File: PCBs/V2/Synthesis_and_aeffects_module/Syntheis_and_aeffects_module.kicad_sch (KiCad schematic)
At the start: 36 parts, among them J1(AudioJack)1 Conn_01x03, J2(IN)1 IN, J3(OUT)1 OUT, U1 STM32H750VBTx, U2 TPA6110A2DGN

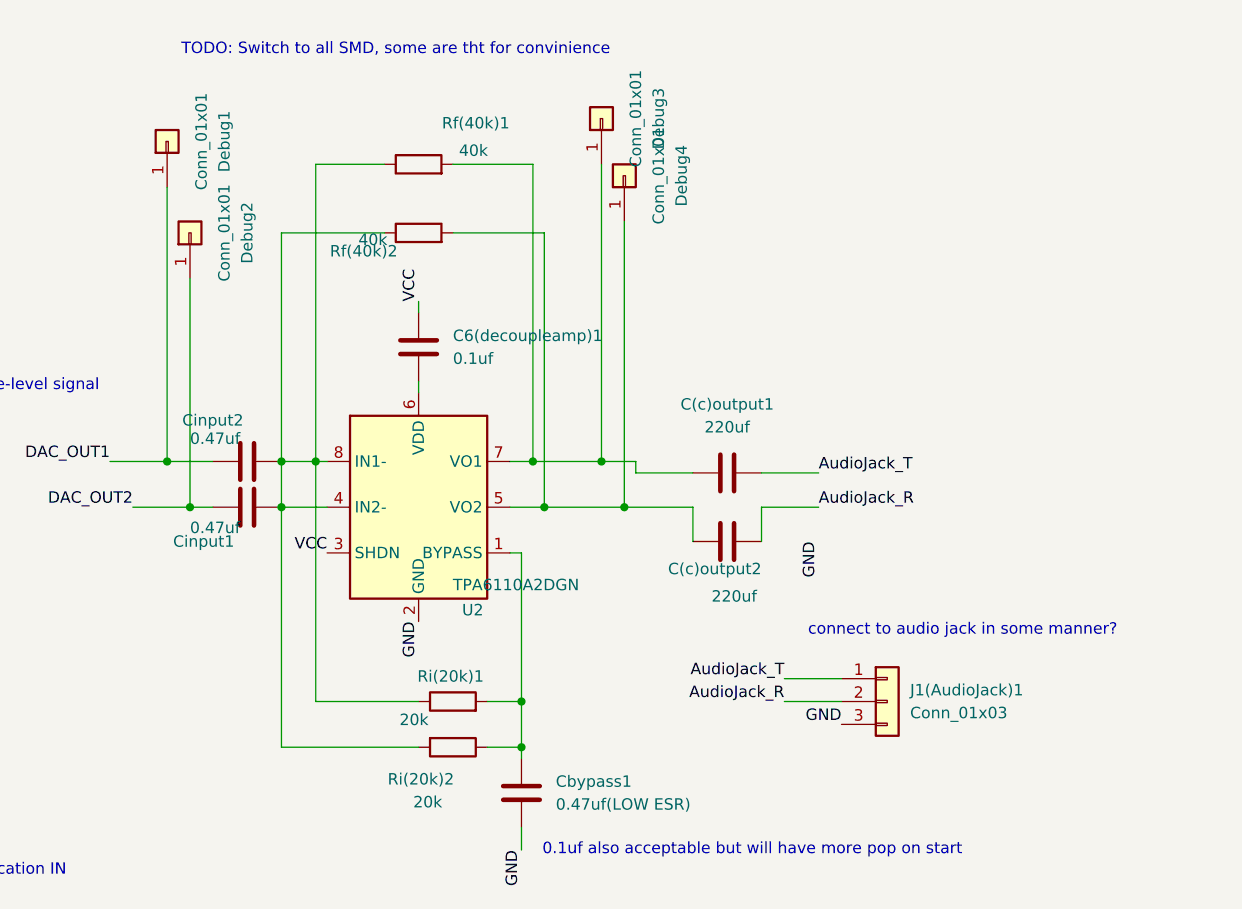
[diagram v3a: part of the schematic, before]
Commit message: more progress on synthesis pcb
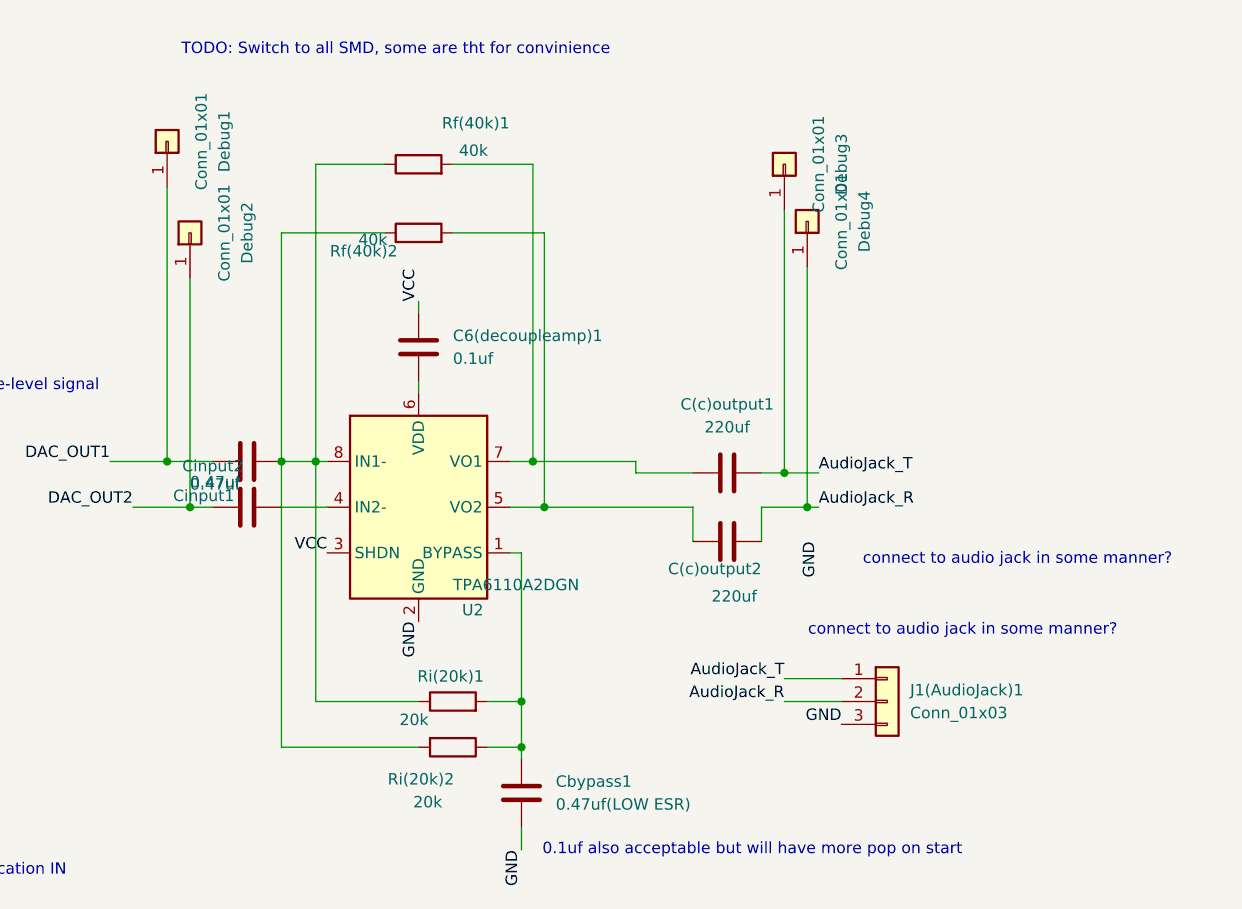
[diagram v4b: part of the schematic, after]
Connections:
- net AudioJack_R: now also Debug4.1 (Pin_1)
- net AudioJack_T: now also Debug3.1 (Pin_1)
- net DAC_OUT1: now also Cinput1.1; no longer Cinput2.1
- net DAC_OUT2: now also Cinput2.1; no longer Cinput1.1
- net at Cinput1.2, Rf(40k)1.1, Rf(40k)2.1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: no longer Cinput2.2, U2.4 (IN2-)
- net at C(c)output1.1, Rf(40k)1.2, U2.7 (VO1): no longer Debug3.1 (Pin_1)
- net at C(c)output2.1, Rf(40k)2.2, U2.5 (VO2): no longer Debug4.1 (Pin_1)
- new net: Cinput2.2, U2.4 (IN2-)
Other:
- moved on the sheet: Cinput1, Cinput2, Debug3, Debug4
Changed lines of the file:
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@@
 		)
 	)
+	(text "connect to audio jack in some manner?\n"
+		(exclude_from_sim no)
+		(at 283.718 79.502 0)
+		(effects
+			(font
+				(size 1.27 1.27)
+			)
+		)
+	)
 	(text "TODO: Switch to all SMD, some are tht for convinience\n"
 		(exclude_from_sim no)
@@
 	)
 	(junction
-		(at 201.93 73.66)
+		(at 201.93 68.58)
 		(diameter 0)
 		(color 0 0 0 0)
@@
 	)
 	(junction
-		(at 205.74 68.58)
+		(at 260.35 73.66)
 		(diameter 0)
 		(color 0 0 0 0)
 	)
 	(junction
-		(at 201.93 68.58)
+		(at 205.74 68.58)
 		(diameter 0)
 		(color 0 0 0 0)
 	)
 	(junction
-		(at 237.49 68.58)
+		(at 257.81 69.85)
 		(diameter 0)
 		(color 0 0 0 0)
@@
 	)
 	(junction
-		(at 240.03 73.66)
-		(diameter 0)
-		(color 0 0 0 0)
-	)
-	(junction
 		(at 69.85 168.91)
 		(diameter 0)
@@
 	(wire
 		(pts
+			(xy 260.35 46.99) (xy 260.35 73.66)
+		)
+		(stroke
+			(width 0)
+			(type default)
+		)
+	)
+	(wire
+		(pts
 			(xy 107.95 31.75) (xy 107.95 36.83)
 		)
@@
 	(wire
 		(pts
+			(xy 257.81 40.64) (xy 257.81 69.85)
+		)
+		(stroke
+			(width 0)
+			(type default)
+		)
+	)
+	(wire
+		(pts
 			(xy 227.33 73.66) (xy 231.14 73.66)
 		)
@@
 	(wire
 		(pts
-			(xy 255.27 69.85) (xy 261.62 69.85)
+			(xy 255.27 69.85) (xy 257.81 69.85)
 		)
 		(stroke
@@
 	(wire
 		(pts
-			(xy 240.03 73.66) (xy 247.65 73.66)
+			(xy 257.81 92.71) (xy 264.16 92.71)
 		)
 		(stroke
@@
 	(wire
 		(pts
-			(xy 257.81 92.71) (xy 264.16 92.71)
+			(xy 260.35 73.66) (xy 261.62 73.66)
 		)
 		(stroke
@@
 	(wire
 		(pts
+			(xy 201.93 43.18) (xy 201.93 68.58)
+		)
+		(stroke
+			(width 0)
+			(type default)
+		)
+	)
+	(wire
+		(pts
 			(xy 60.96 165.1) (xy 60.96 168.91)
 		)
@@
 	(wire
 		(pts
-			(xy 201.93 43.18) (xy 201.93 68.58)
+			(xy 257.81 69.85) (xy 261.62 69.85)
 		)
 		(stroke
@@
 	(wire
 		(pts
-			(xy 255.27 73.66) (xy 261.62 73.66)
+			(xy 255.27 73.66) (xy 260.35 73.66)
 		)
 		(stroke
@@
 	(wire
 		(pts
-			(xy 237.49 35.56) (xy 237.49 68.58)
-		)
-		(stroke
-			(width 0)
-			(type default)
-		)
-	)
-	(wire
-		(pts
 			(xy 227.33 78.74) (xy 228.6 78.74)
 		)
@@
 	(wire
 		(pts
-			(xy 237.49 68.58) (xy 241.3 68.58)
-		)
-		(stroke
-			(width 0)
-			(type default)
-		)
-	)
-	(wire
-		(pts
 			(xy 49.53 46.99) (xy 53.34 46.99)
 		)
@@
 	(wire
 		(pts
-			(xy 231.14 73.66) (xy 240.03 73.66)
+			(xy 231.14 73.66) (xy 247.65 73.66)
 		)
 		(stroke
@@
 	(wire
 		(pts
-			(xy 201.93 68.58) (xy 201.93 73.66)
+			(xy 95.25 31.75) (xy 95.25 36.83)
 		)
 		(stroke
@@
 	(wire
 		(pts
-			(xy 95.25 31.75) (xy 95.25 36.83)
+			(xy 201.93 68.58) (xy 205.74 68.58)
 		)
 		(stroke
@@
 	(wire
 		(pts
-			(xy 201.93 68.58) (xy 205.74 68.58)
+			(xy 201.93 68.58) (xy 201.93 100.33)
 		)
 		(stroke
@@
 	(wire
 		(pts
-			(xy 201.93 73.66) (xy 201.93 100.33)
-		)
-		(stroke
-			(width 0)
-			(type default)
-		)
-	)
-	(wire
-		(pts
-			(xy 240.03 41.91) (xy 240.03 73.66)
-		)
-		(stroke
-			(width 0)
-			(type default)
-		)
-	)
-	(wire
-		(pts
 			(xy 217.17 52.07) (xy 217.17 50.8)
 		)
@@
 	(wire
 		(pts
-			(xy 229.87 68.58) (xy 237.49 68.58)
+			(xy 229.87 68.58) (xy 241.3 68.58)
 		)
 		(stroke
@@
 	(symbol
 		(lib_id "Connector_Generic:Conn_01x01")
-		(at 240.03 36.83 90)
+		(at 260.35 41.91 90)
 		(unit 1)
 		(exclude_from_sim no)
@@
 		(dnp no)
 		(property "Reference" "Debug4"
-			(at 246.38 36.83 0)
+			(at 266.7 41.91 0)
 			(effects
 				(font
@@
 		)
 		(property "Value" "Conn_01x01"
-			(at 243.84 36.83 0)
+			(at 264.16 41.91 0)
 			(effects
 				(font
@@
 		)
 		(property "Footprint" "TestPoint:TestPoint_Pad_1.5x1.5mm"
-			(at 240.03 36.83 0)
+			(at 260.35 41.91 0)
 			(effects
 				(font
@@
 		)
 		(property "Datasheet" "~"
-			(at 240.03 36.83 0)
+			(at 260.35 41.91 0)
 			(effects
 				(font
@@
 		)
 		(property "Description" "Generic connector, single row, 01x01, script generated (kicad-library-utils/schlib/autogen/connector/)"
-			(at 240.03 36.83 0)
+			(at 260.35 41.91 0)
 			(effects
 				(font
@@
 	(symbol
 		(lib_id "Device:C")
-		(at 198.12 73.66 90)
+		(at 198.12 68.58 90)
 		(unit 1)
 		(exclude_from_sim no)
@@
 		(dnp no)
 		(property "Reference" "Cinput1"
-			(at 193.294 77.47 90)
+			(at 193.294 72.39 90)
 			(effects
 				(font
@@
 		)
 		(property "Value" "0.47uf"
-			(at 194.564 75.946 90)
+			(at 194.564 70.866 90)
 			(effects
 				(font
@@
 		)
 		(property "Footprint" "Capacitor_SMD:C_0603_1608Metric_Pad1.08x0.95mm_HandSolder"
-			(at 201.93 72.6948 0)
+			(at 201.93 67.6148 0)
 			(effects
 				(font
@@
 		)
 		(property "Datasheet" "~"
-			(at 198.12 73.66 0)
+			(at 198.12 68.58 0)
 			(effects
 				(font
@@
 		)
 		(property "Description" "Unpolarized capacitor"
-			(at 198.12 73.66 0)
+			(at 198.12 68.58 0)
 			(effects
 				(font
@@
 		)
 		(instances
-			(project ""
+			(project "Syntheis_and_aeffects_module"
 				(path "/edf9ac54-8c23-46ef-867e-bfab8959c07a"
 					(reference "Cinput1")
@@
 	(symbol
 		(lib_id "Device:C")
-		(at 198.12 68.58 90)
+		(at 198.12 73.66 90)
 		(unit 1)
 		(exclude_from_sim no)
@@
 		(dnp no)
 		(property "Reference" "Cinput2"
-			(at 194.31 64.008 90)
+			(at 194.31 69.088 90)
 			(effects
 				(font
@@
 		)
 		(property "Value" "0.47uf"
-			(at 194.564 66.04 90)
+			(at 194.564 71.12 90)
 			(effects
 				(font
@@
 		)
 		(property "Footprint" "Capacitor_SMD:C_0603_1608Metric_Pad1.08x0.95mm_HandSolder"
-			(at 201.93 67.6148 0)
+			(at 201.93 72.6948 0)
 			(effects
 				(font
@@
 		)
 		(property "Datasheet" "~"
-			(at 198.12 68.58 0)
+			(at 198.12 73.66 0)
 			(effects
 				(font
@@
 		)
 		(property "Description" "Unpolarized capacitor"
-			(at 198.12 68.58 0)
+			(at 198.12 73.66 0)
 			(effects
 				(font
@@
 	(symbol
 		(lib_id "Connector_Generic:Conn_01x01")
-		(at 237.49 30.48 90)
+		(at 257.81 35.56 90)
 		(unit 1)
 		(exclude_from_sim no)
@@
 		(dnp no)
 		(property "Reference" "Debug3"
-			(at 243.84 30.48 0)
+			(at 264.16 35.56 0)
 			(effects
 				(font
@@
 		)
 		(property "Value" "Conn_01x01"
-			(at 241.3 30.48 0)
+			(at 261.62 35.56 0)
 			(effects
 				(font
@@
 		)
 		(property "Footprint" "TestPoint:TestPoint_Pad_1.5x1.5mm"
-			(at 237.49 30.48 0)
+			(at 257.81 35.56 0)
 			(effects
 				(font
@@
 		)
 		(property "Datasheet" "~"
-			(at 237.49 30.48 0)
+			(at 257.81 35.56 0)
 			(effects
 				(font
@@
 		)
 		(property "Description" "Generic connector, single row, 01x01, script generated (kicad-library-utils/schlib/autogen/connector/)"
-			(at 237.49 30.48 0)
+			(at 257.81 35.56 0)
 			(effects
 				(font

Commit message: some updates
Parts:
- removed Debug3, Debug4: Conn_01x01, TestPoint:TestPoint_Pad_1.5x1.5mm, symbol Connector_Generic:Conn_01x01
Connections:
- net GNDPWR: now also C6(decoupleamp)1.1, U2.3 (SHDN)
- net VCC: now also C6(decoupleamp)1.2, U2.6 (VDD); no longer C6(decoupleamp)1.1, U2.3 (SHDN)
- net at Cbypass1.1, U2.1 (BYPASS): no longer Ri(20k)1.2, Ri(20k)2.1
- net at U2.4 (IN2-): now also Rf(40k)2.1, Ri(20k)2.1; no longer Cinput2.2
- new net: Rf(40k)1.1, Ri(20k)1.2, U2.8 (IN1-)
- new net: Cinput1.2, Ri(20k)1.1
- new net: Cinput2.2, Ri(20k)2.2
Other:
- note added: "connect to audio jack in some manner (eg out pins)"
- note removed: "TODO: Switch to all SMD, some are tht for convinience"
- note removed: "connect to audio jack in some manner?"
- moved on the sheet: Cbypass1, Cinput1, Cinput2, Debug1, Debug2, Ri(20k)1, Ri(20k)2
